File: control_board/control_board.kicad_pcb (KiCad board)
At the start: 2 copper layers, 51.2 x 76.2 mm, 41 parts, among them J1 Conn_01x08_Male, K1 G5Q-1A, Q1 Q_NPN_BEC, U1 MC78M05_TO252, U2 TSR_1-24120, U3 74LS02, U4 74LS02, U5 Conn_01x08_Male

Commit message: Draft layout
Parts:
- D1, D3, L1: moved to B.Cu
- moved C12 99.6 mm to (101.1, 85.3)
- moved D1 50.0 mm to (134.7, 36.1)
- moved U1 38.7 mm to (117.4, 68.6), turned to 180 degrees
- moved D2 28.4 mm to (118.2, 75.1), turned to 0 degrees
- moved C3 20.9 mm to (135.6, 49.7)
- moved C2 19.9 mm to (117.8, 46.2), turned to 0 degrees
- moved F4 17.3 mm to (132.5, 46.2), turned to 180 degrees
- moved D3 15.2 mm to (147.1, 63.5)
- moved F3 13.7 mm to (124.0, 30.1), turned to 90 degrees
- moved K1 11.7 mm to (150.9, 63.5)
- moved F2 10.8 mm to (146.3, 41.1)
- moved L1 10.7 mm to (124.0, 40.1), turned to 270 degrees
- moved RV1 10.3 mm to (141.7, 41.7)
- moved F1 9.90 mm to (146.3, 36.6)
- moved U2 8.82 mm to (136.1, 40.6), turned to 180 degrees
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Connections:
- F1 pad 1: /hv_03 -> /hv_02
- F2 pad 1: /hv_02 -> /hv_03
- RV1 pad 1: /hv_02 -> /hv_03
- RV1 pad 2: /hv_03 -> /hv_02
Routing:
- net +12V: track 87.2 -> 26.1 mm, vias 3 -> 1
- net +5V: track 119.2 -> 77.1 mm, vias 1 -> 0
- net /contactor_b: track 39.4 -> 0.00 mm
- net /hv_06: track 35.8 -> 0.00 mm
- net /hv_03: track 15.0 -> 0.00 mm
- net /hv_02: track 12.6 -> 0.00 mm
- net /hc_01: track 12.3 -> 0.00 mm
- net /hv_04: track 12.1 -> 0.00 mm, vias 2 -> 0
- net /hv_05: track 8.27 -> 0.00 mm, vias 1 -> 0
- net /sensor_a: track 77.6 -> 69.6 mm
- net /hv_07: track 5.99 -> 0.00 mm
- net /pot_a: track 74.4 -> 68.9 mm
- net GNDPWR: track 3.96 -> 0.00 mm
- net AC: track 0.97 -> 0.00 mm
- net GND: track 3.88 -> 3.00 mm, vias 2 -> 0

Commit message: Draft logic layout
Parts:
- C10, C11, C12, C5, C6, C7, C8, C9, U3, U4, U5: moved to B.Cu
- moved C6 35.0 mm to (132.6, 60.5), turned to 0 degrees
- moved RN2 31.0 mm to (122.3, 61.8)
- moved C11 28.7 mm to (115.3, 67.6)
- moved U3 27.9 mm to (133.6, 66.5), turned to 180 degrees
- moved D2 27.6 mm to (135.8, 53.9)
- moved C5 27.4 mm to (118.9, 71.1)
- moved RN1 20.9 mm to (136.3, 76.9), turned to 270 degrees
- moved Q1 20.6 mm to (146.8, 59.0), turned to 0 degrees
- moved U5 19.2 mm to (114.8, 72.6), turned to 270 degrees
- moved U1 17.8 mm to (118.4, 50.8)
- moved U4 17.4 mm to (123.9, 73.9)
- moved C12 16.1 mm to (115.3, 77.7)
- moved RN3 7.78 mm to (147.8, 72.6)
- moved C9 1.30 mm to (146.8, 87.4)
- moved C10 1.30 mm to (144.3, 87.4)
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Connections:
- A1 pad 10: /aref_1k1 -> /th1_tap
- A1 pad 11: /aref_1k2 -> /th2_tap
- A1 pad 8: /th1_tap -> /aref_1k1
- A1 pad 9: /th2_tap -> /aref_1k2
- RN1 pad 1: /p_cmd -> /p_rqst
- RN1 pad 10: /th1_tap -> /th2_tap
- RN1 pad 12: /th2_tap -> /th1_tap
- RN1 pad 13: Net-(A1-Pad18) -> Net-(RN1-Pad13)
- RN1 pad 14: Net-(A1-Pad18) -> /aref_1k2
- RN1 pad 15: Net-(Q1-Pad1) -> /aref_1k1
- RN1 pad 16: Net-(Q1-Pad1) -> GND
- RN1 pad 2: GND -> Net-(A1-Pad18)
- RN1 pad 3: /raref_1k2 -> Net-(A1-Pad18)
- RN1 pad 4: /aref_1k1 -> Net-(RN1-Pad4)
- RN1 pad 6: +5V -> Net-(A1-Pad21)
- RN1 pad 7: Net-(A1-Pad21) -> +5V
- RN1 pad 8: /th2_tap -> /sensor_a
- RN1 pad 9: /sensor_a -> /th2_tap
- RN2 pad 1: /p_rqst -> /p_cmd
- RN2 pad 10: +5V -> GND
- RN2 pad 13: +5V -> GND
- RN2 pad 14: GND -> +5V
- RN2 pad 15: GND -> Net-(Q1-Pad1)
- RN2 pad 16: GND -> Net-(Q1-Pad1)
- RN2 pad 2: /sr_rst -> GND
- RN2 pad 3: /wd_kick -> Net-(RN2-Pad3)
- RN2 pad 5: Net-(RN2-Pad5) -> /sr_rst
- RN2 pad 7: Net-(RN2-Pad7) -> /wd_kick
- RN3 pad 1: Net-(RN3-Pad1) -> /pot_a
- RN3 pad 10: Net-(A1-Pad18) -> Net-(RN3-Pad10)
- RN3 pad 11: Net-(D6-Pad2) -> Net-(RN3-Pad10)
- RN3 pad 13: Net-(RN3-Pad1) -> Net-(D5-Pad2)
- RN3 pad 15: Net-(D5-Pad2) -> /aref_330
- RN3 pad 16: Net-(D4-Pad2) -> +5V
- RN3 pad 2: Net-(RN3-Pad2) -> Net-(A1-Pad18)
- RN3 pad 3: Net-(RN3-Pad2) -> Net-(RN3-Pad3)
- RN3 pad 4: +12V -> Net-(RN3-Pad3)
- RN3 pad 5: +12V -> Net-(D4-Pad2)
- RN3 pad 6: Net-(RN3-Pad12) -> Net-(D6-Pad2)
- RN3 pad 7: /aref_330 -> +12V
- RN3 pad 8: +5V -> +12V
- RN3 pad 9: /pot_a -> Net-(RN3-Pad12)
- U3 pad 1: Net-(RN3-Pad2) -> Net-(U3-Pad1)
- U3 pad 10: /p_cmd -> Net-(RN3-Pad3)
- U3 pad 11: Net-(RN3-Pad2) -> Net-(U3-Pad11)
- U3 pad 12: Net-(RN3-Pad2) -> Net-(U3-Pad1)
- U3 pad 13: Net-(U3-Pad13) -> /p_cmd
- U3 pad 2: Net-(RN2-Pad4) -> Net-(RN3-Pad3)
- U3 pad 3: /sr_rst -> Net-(RN3-Pad3)
- U3 pad 4: Net-(U3-Pad4) -> Net-(U3-Pad11)
- U3 pad 8: Net-(U3-Pad13) -> /sr_rst
- U3 pad 9: Net-(U3-Pad4) -> Net-(RN2-Pad3)
- U4 pad 1: Net-(RN2-Pad4) -> Net-(RN2-Pad3)
- U4 pad 3: Net-(RN2-Pad5) -> Net-(RN2-Pad4)
- U4 pad 4: Net-(RN2-Pad5) -> Net-(RN2-Pad4)
- U4 pad 5: Net-(RN2-Pad4) -> Net-(RN2-Pad3)
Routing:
- net +5V: track 77.1 -> 14.1 mm
- net /pot_a: track 68.9 -> 11.2 mm, vias 2 -> 0
- net /sensor_a: track 69.6 -> 15.2 mm, vias 1 -> 0
- net Net-(A1-Pad21): track 53.5 -> 15.2 mm
- net Net-(RN3-Pad2): track 35.7 -> 0.00 mm, vias 1 -> 0
- net /wd_kick: track 15.7 -> 43.6 mm
- net /aref_330: track 0.00 -> 27.6 mm
- net /sr_rst: track 30.0 -> 55.4 mm
- net Net-(RN3-Pad3): track 0.00 -> 22.7 mm
- net /aref_1k2: track 0.00 -> 21.4 mm
- net /aref_1k1: track 0.00 -> 21.0 mm
- net /th1_tap: track 1.27 -> 22.3 mm
- net /p_rqst: track 18.4 -> 36.5 mm
- net Net-(D6-Pad2): track 17.9 -> 0.00 mm, vias 1 -> 0
- net Net-(RN2-Pad3): track 0.00 -> 17.8 mm
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
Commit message: Layout almost done
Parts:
- added C13: 2.2u, Capacitor_SMD:C_0805_2012Metric_Pad1.18x1.45mm_HandSolder, B.Cu at (119.9, 45.7)
- added C14: 2.2u, Capacitor_SMD:C_0805_2012Metric_Pad1.18x1.45mm_HandSolder, B.Cu at (119.9, 55.9)
- moved C3 19.0 mm to (134.6, 68.6)
- moved C2 17.3 mm to (134.1, 40.6), turned to 90 degrees
- moved F4 15.2 mm to (143.3, 57.0), turned to 90 degrees
- moved U2 11.2 mm to (137.2, 51.8), turned to 270 degrees
- moved D2 7.49 mm to (137.2, 46.6), turned to 90 degrees
- moved C1 6.26 mm to (120.4, 54.5), turned to 270 degrees
- moved C4 3.35 mm to (120.0, 73.2)
- moved Q1 3.10 mm to (149.9, 58.9)
- moved D1 0.68 mm to (134.1, 36.5), turned to 270 degrees
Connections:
- D2 pad 1: +5V -> /pot_a
- D2 pad 3: /sensor_a -> +5V
- D2 pad 5: /pot_a -> /sensor_a
- RN1 pad 4: Net-(RN1-Pad4) -> +5V
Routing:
- net +5V: track 14.1 -> 99.9 mm, vias 0 -> 2
- net /pot_a: track 11.2 -> 75.5 mm, vias 0 -> 1
- net /sensor_a: track 15.2 -> 77.3 mm, vias 0 -> 1
- net +12V: track 9.06 -> 49.7 mm, vias 0 -> 1
- net Net-(A1-Pad21): track 15.2 -> 51.0 mm
- net /hv_04: track 0.00 -> 34.6 mm, vias 0 -> 1
- net /contactor_b: track 0.00 -> 26.3 mm
- net AC: track 0.00 -> 24.4 mm
- net Net-(D6-Pad2): track 0.00 -> 19.8 mm, vias 0 -> 1
- net Net-(D4-Pad2): track 0.00 -> 19.6 mm, vias 0 -> 1
- net /hv_06: track 0.00 -> 19.3 mm, vias 0 -> 1
- net /hc_05: track 7.09 -> 26.2 mm
- net /hv_03: track 0.00 -> 15.3 mm
- net GNDPWR: track 0.00 -> 12.3 mm
- net /hv_02: track 0.00 -> 11.4 mm
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
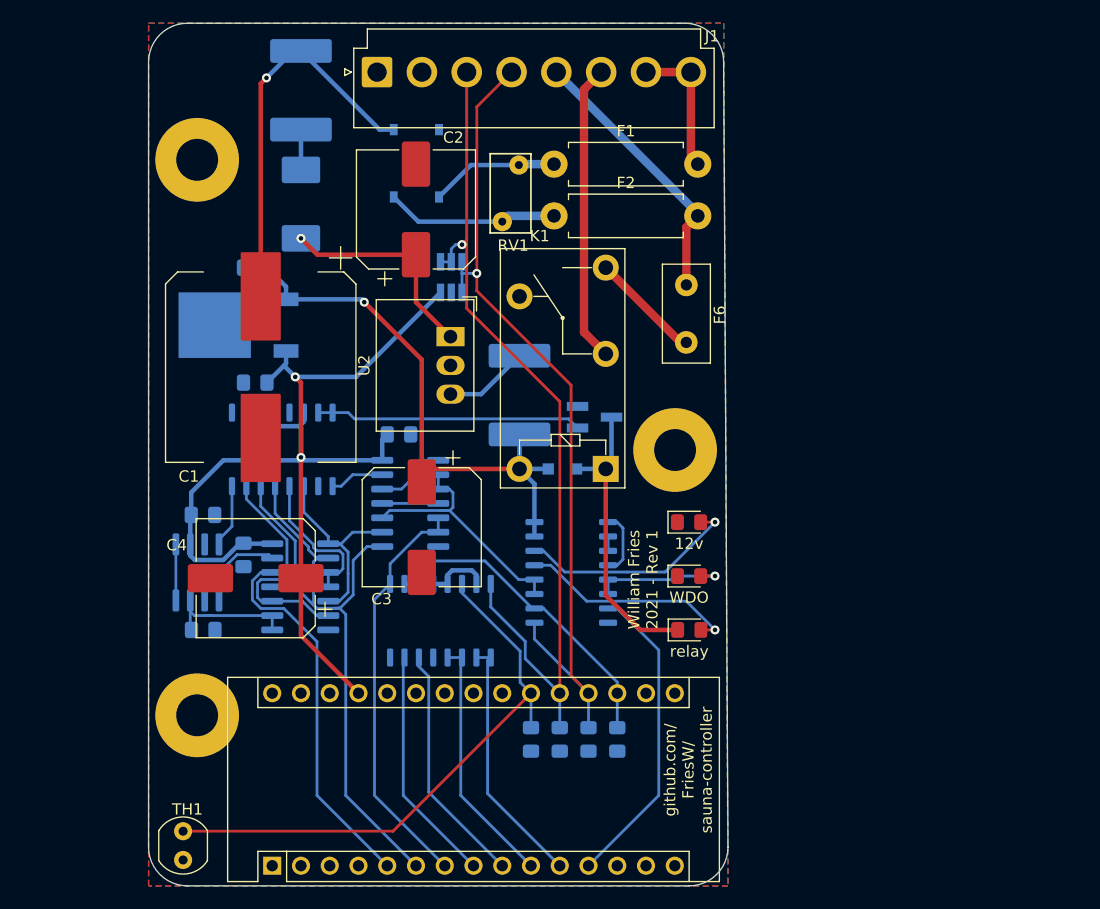
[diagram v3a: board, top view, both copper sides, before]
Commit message: Layout complete
TODO
Via stitch ground
Fix silkscreen positions
Final check of revision notes
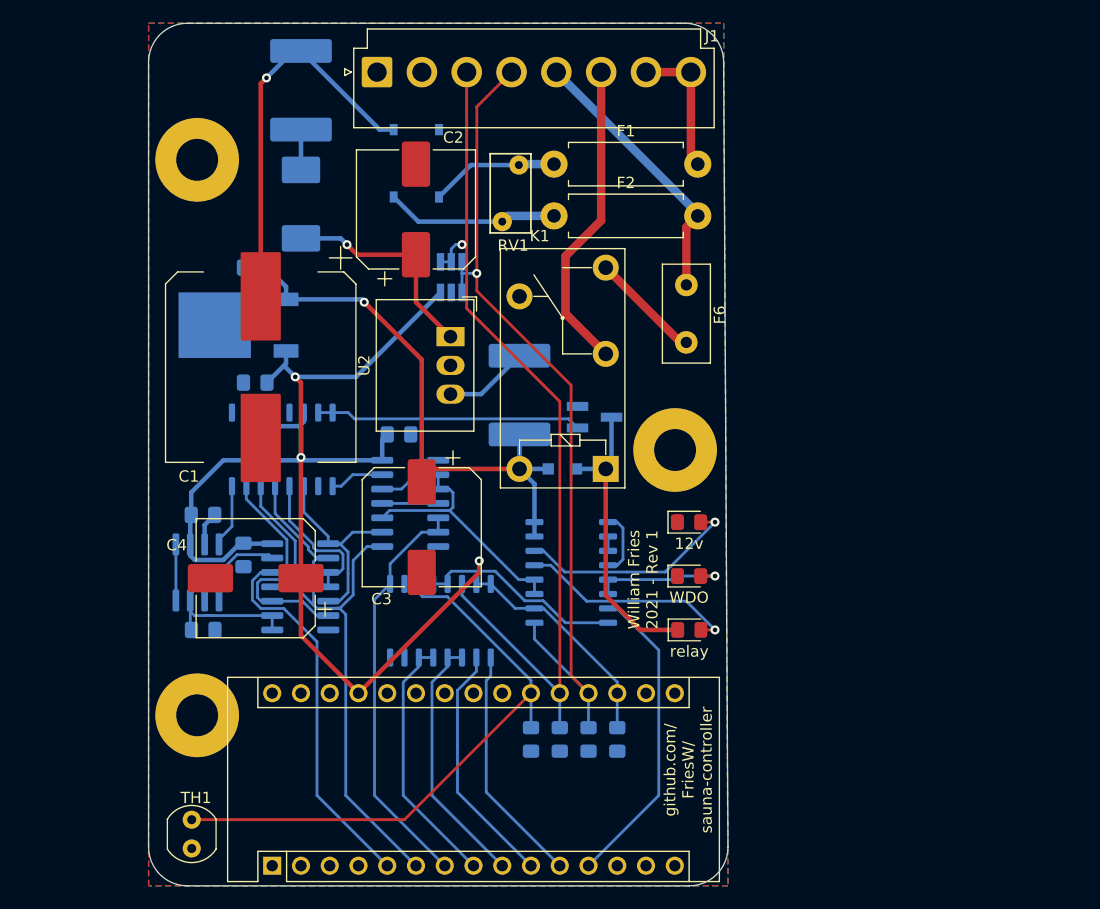
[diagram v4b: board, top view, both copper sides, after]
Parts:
- moved TH1 1.27 mm to (114.3, 94.5)
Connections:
- A1 pad 10: /th1_tap -> /aref_1k2
- A1 pad 11: /th2_tap -> /aref_1k1
- A1 pad 8: /aref_1k1 -> /th1_tap
- A1 pad 9: /aref_1k2 -> /th2_tap
- RN1 pad 10: /th2_tap -> /aref_1k2
- RN1 pad 11: /th1_tap -> /th2_tap
- RN1 pad 12: /th1_tap -> /th2_tap
- RN1 pad 13: Net-(RN1-Pad13) -> /th1_tap
- RN1 pad 14: /aref_1k2 -> /th1_tap
- RN1 pad 15: /aref_1k1 -> GND
- RN1 pad 2: Net-(A1-Pad18) -> Net-(RN1-Pad2)
- RN1 pad 3: Net-(A1-Pad18) -> Net-(A1-Pad21)
- RN1 pad 6: Net-(A1-Pad21) -> /sensor_a
- RN1 pad 7: +5V -> Net-(A1-Pad18)
- RN1 pad 8: /sensor_a -> Net-(A1-Pad18)
- RN1 pad 9: /th2_tap -> /aref_1k1
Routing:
- net +5V: track 99.9 -> 129.4 mm, vias 2 -> 3
- net Net-(A1-Pad18): track 28.6 -> 20.1 mm
- net GND: track 0.00 -> 2.97 mm
- net Net-(A1-Pad21): track 51.0 -> 52.7 mm
- net /contactor_b: track 26.3 -> 27.7 mm
- net /sensor_a: track 77.3 -> 78.3 mm
- net /th1_tap: track 22.3 -> 22.8 mm

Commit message: PCB Rev2 Complete
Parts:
- moved C10 1.52 mm to (142.7, 87.4)
- moved C7 1.52 mm to (153.4, 87.4)
- moved C8 0.51 mm to (149.9, 87.4)
- moved C9 0.51 mm to (146.3, 87.4)
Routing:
- net GND: track 2.97 -> 10.5 mm, vias 0 -> 129
- net Net-(D4-Pad2): track 19.6 -> 17.8 mm
- net /pot_a: track 75.5 -> 76.7 mm
- net Net-(Q1-Pad1): track 23.5 -> 24.4 mm
- net Net-(A1-Pad21): track 52.7 -> 53.6 mm
- net Net-(D5-Pad2): track 12.1 -> 11.3 mm
- net +5V: track 129.4 -> 128.7 mm
- net Net-(A1-Pad18): track 20.1 -> 20.7 mm
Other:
- rule trace_min: 0.2 -> 0
- board text added: "DGND DGND 330kΩ NTC 300Ω POT 24V AC IN SW AC OUT ACGND ACGND"
- board text added: "William Fries 2021 - Rev 2"
- board text removed: "William Fries 2021 - Rev 1"

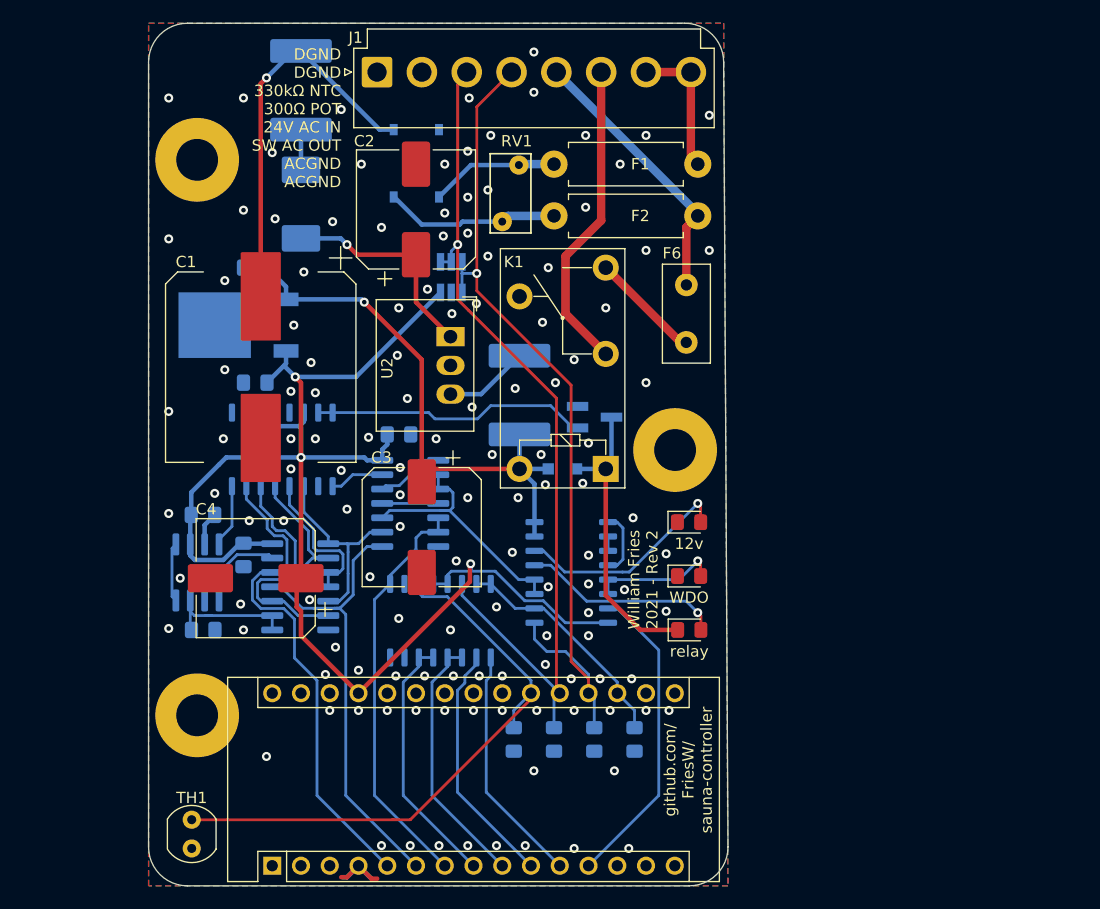
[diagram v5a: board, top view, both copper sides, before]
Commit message: Via & trace tweaks
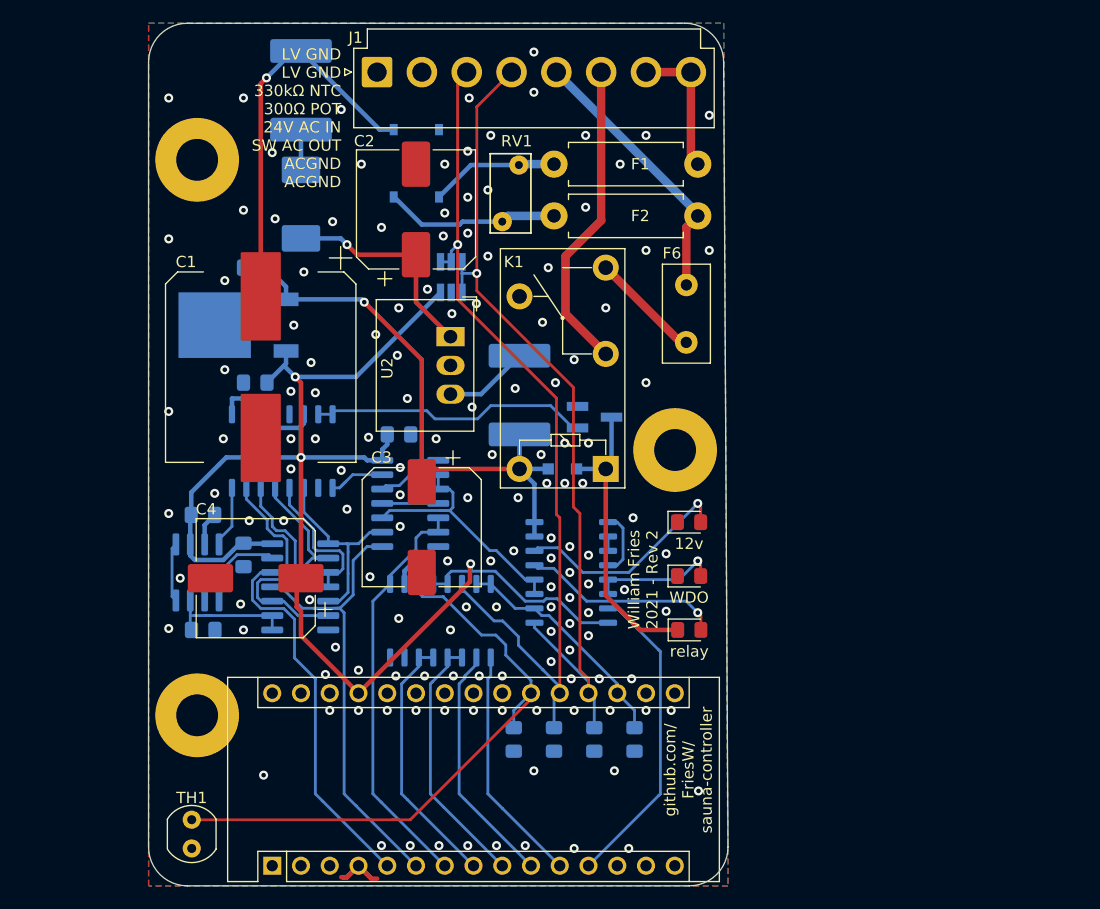
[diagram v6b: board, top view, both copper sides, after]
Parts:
- moved RN2 0.15 mm to (122.3, 61.9)
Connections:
- RN1 pad 2: Net-(RN1-Pad2) -> GND
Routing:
- net GND: track 10.5 -> 19.2 mm, vias 129 -> 143
- net /pot_a: track 76.7 -> 75.7 mm
- net /p_cmd: track 4.80 -> 5.36 mm
- net Net-(A1-Pad21): track 53.6 -> 54.2 mm
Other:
- board text added: "LV GND LV GND 330kΩ NTC 300Ω POT 24V AC IN SW AC OUT ACGND ACGND"
- board text removed: "DGND DGND 330kΩ NTC 300Ω POT 24V AC IN SW AC OUT ACGND ACGND"

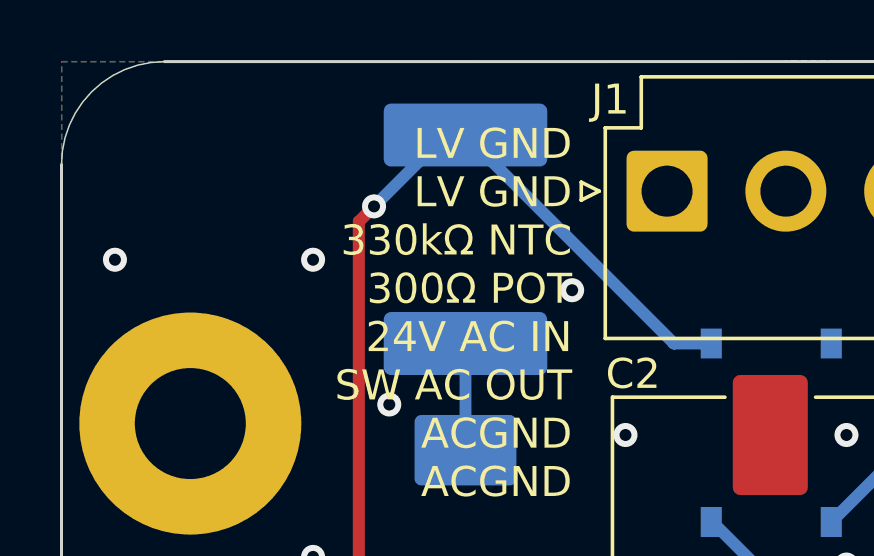
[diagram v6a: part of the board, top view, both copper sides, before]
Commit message: Fix silkscreen typo
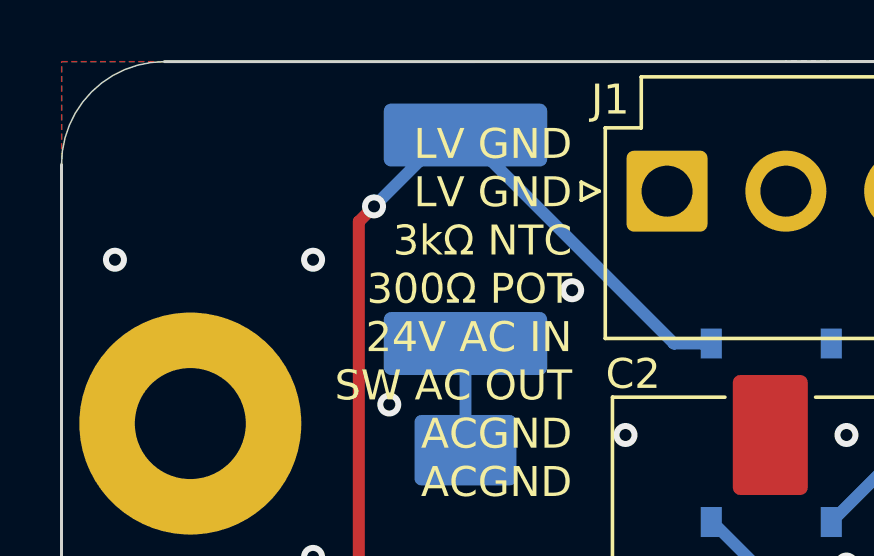
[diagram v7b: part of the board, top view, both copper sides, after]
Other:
- board text added: "LV GND LV GND 3kΩ NTC 300Ω POT 24V AC IN SW AC OUT ACGND ACGND"
- board text removed: "LV GND LV GND 330kΩ NTC 300Ω POT 24V AC IN SW AC OUT ACGND ACGND"
